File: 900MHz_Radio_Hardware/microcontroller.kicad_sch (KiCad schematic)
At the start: 7 parts, among them J1 RJ45_LED_Shielded, SW2 SW_SPDT, U2 Teensy4.1_DEV-16771, U7 MCP4725xxx-xCH

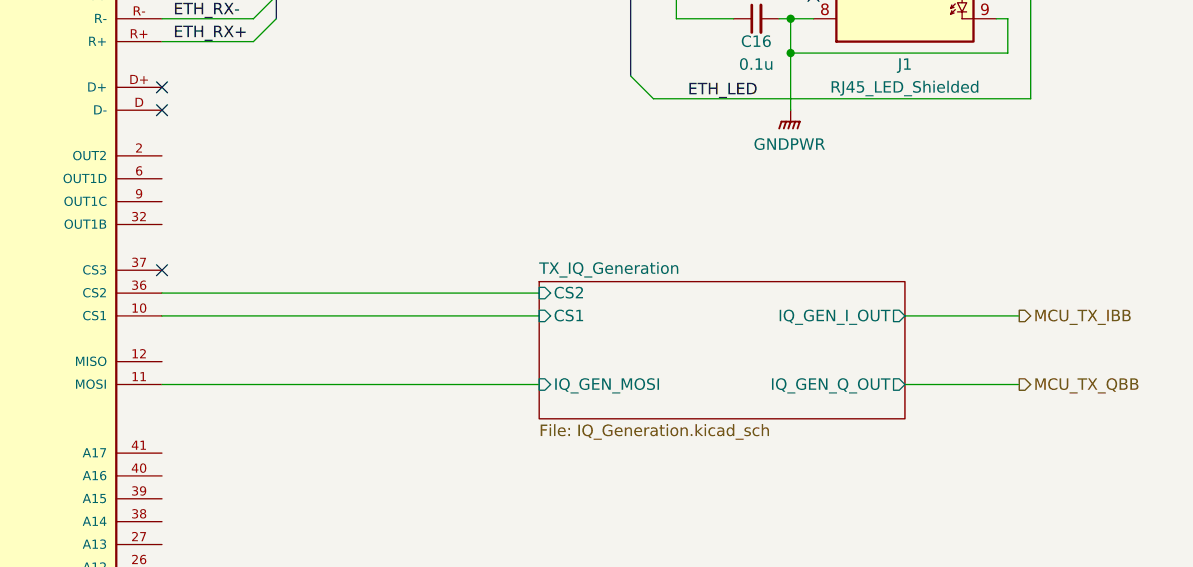
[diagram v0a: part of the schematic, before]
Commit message: Added modulator enable signal
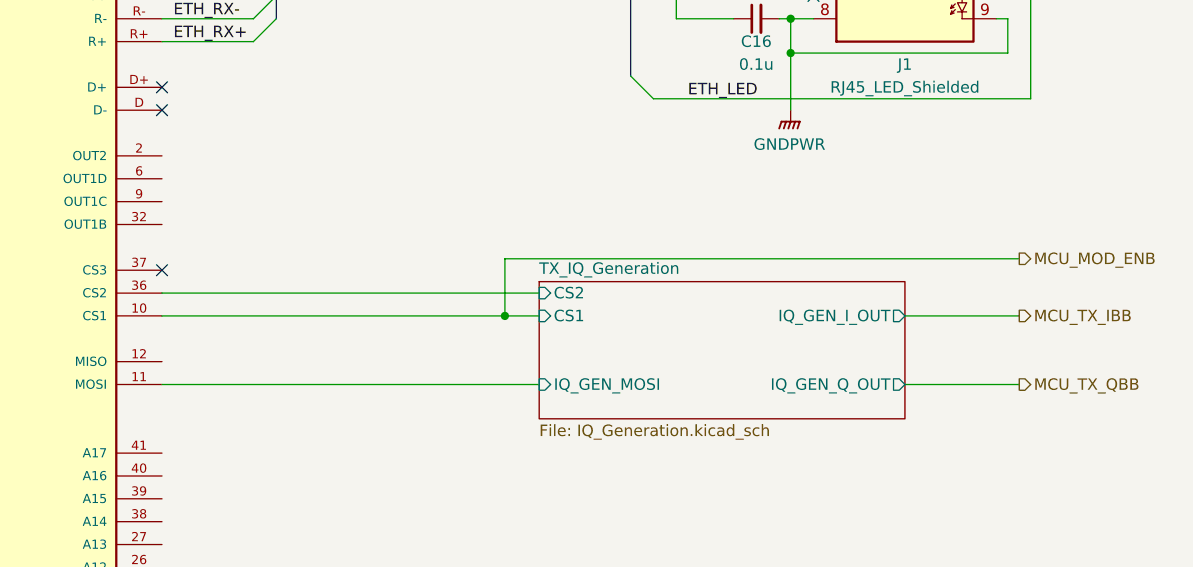
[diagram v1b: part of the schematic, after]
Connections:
- net TX_IQ_Generation/CS1 renamed MCU_MOD_ENB
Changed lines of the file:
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@@
   (junction (at 93.98 101.6) (diameter 0) (color 0 0 0 0)
+  )
+  (junction (at 205.74 76.2) (diameter 0) (color 0 0 0 0)
   )
   (junction (at 237.49 43.18) (diameter 0) (color 0 0 0 0)
@@
     (stroke (width 0) (type default))
   )
+  (wire (pts (xy 262.89 69.85) (xy 205.74 69.85))
+    (stroke (width 0) (type default))
+  )
   (wire (pts (xy 167.64 73.66) (xy 209.55 73.66))
     (stroke (width 0) (type default))
@@
     (stroke (width 0) (type default))
   )
+  (wire (pts (xy 205.74 76.2) (xy 209.55 76.2))
+    (stroke (width 0) (type default))
+  )
   (wire (pts (xy 236.22 43.18) (xy 237.49 43.18))
     (stroke (width 0) (type default))
@@
     (stroke (width 0) (type default))
   )
+  (wire (pts (xy 205.74 69.85) (xy 205.74 76.2))
+    (stroke (width 0) (type default))
+  )
   (wire (pts (xy 250.19 83.82) (xy 262.89 83.82))
     (stroke (width 0) (type default))
@@
     (stroke (width 0) (type default))
   )
-  (wire (pts (xy 167.64 76.2) (xy 209.55 76.2))
+  (wire (pts (xy 167.64 76.2) (xy 205.74 76.2))
     (stroke (width 0) (type default))
   )
@@
     (effects (font (size 1.27 1.27)) (justify right))
   )
+  (hierarchical_label "MCU_MOD_ENB" (shape output) (at 262.89 69.85 0) (fields_autoplaced)
+    (effects (font (size 1.27 1.27)) (justify left))
+  )
   (hierarchical_label "MCU_TX_QBB" (shape output) (at 262.89 83.82 0) (fields_autoplaced)

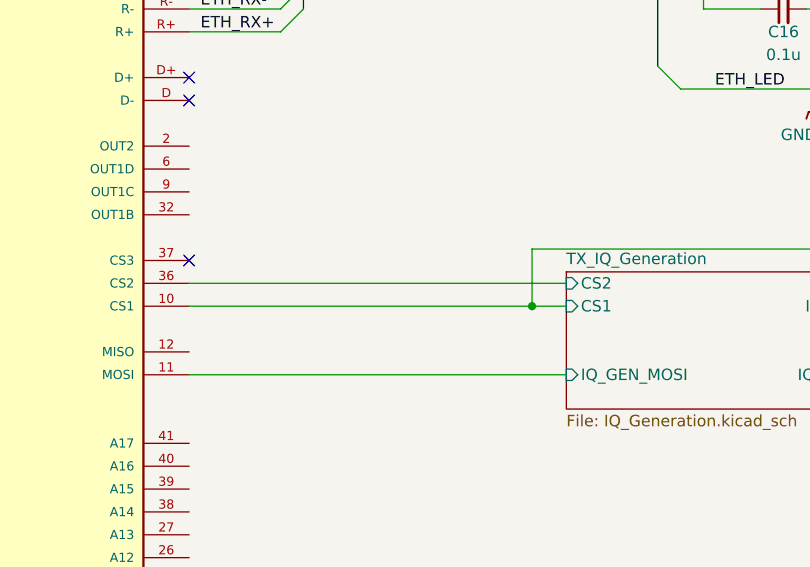
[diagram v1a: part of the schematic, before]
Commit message: Started fixing IQ gen circuit
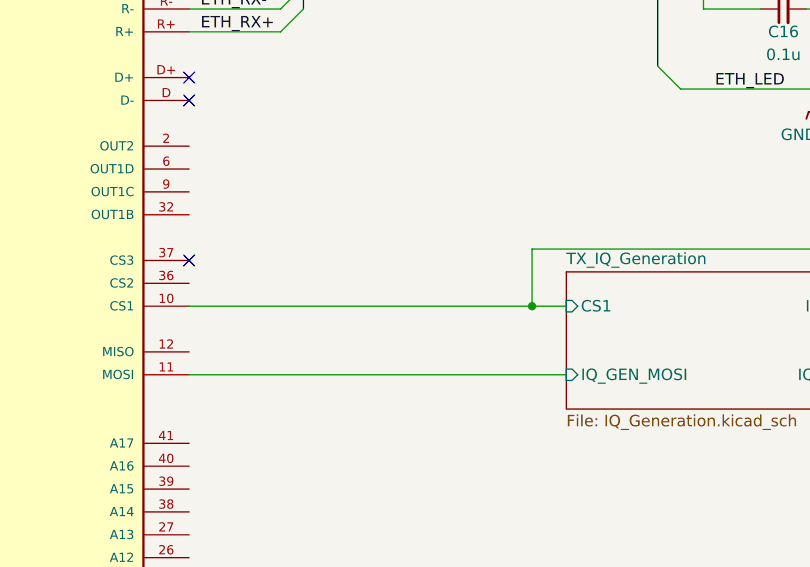
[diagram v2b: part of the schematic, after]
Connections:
- net TX_IQ_Generation/CS2: no longer names the net of U2.36 (CS2)
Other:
- sheet TX_IQ_Generation ports: added none; removed CS2
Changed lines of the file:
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@@
-    (stroke (width 0) (type default))
-  )
-  (wire (pts (xy 167.64 73.66) (xy 209.55 73.66))
     (stroke (width 0) (type default))
   )
@@
       (effects (font (size 1.27 1.27)) (justify left))
     )
-    (pin "CS2" input (at 209.55 73.66 180)
-      (effects (font (size 1.27 1.27)) (justify left))
-    )

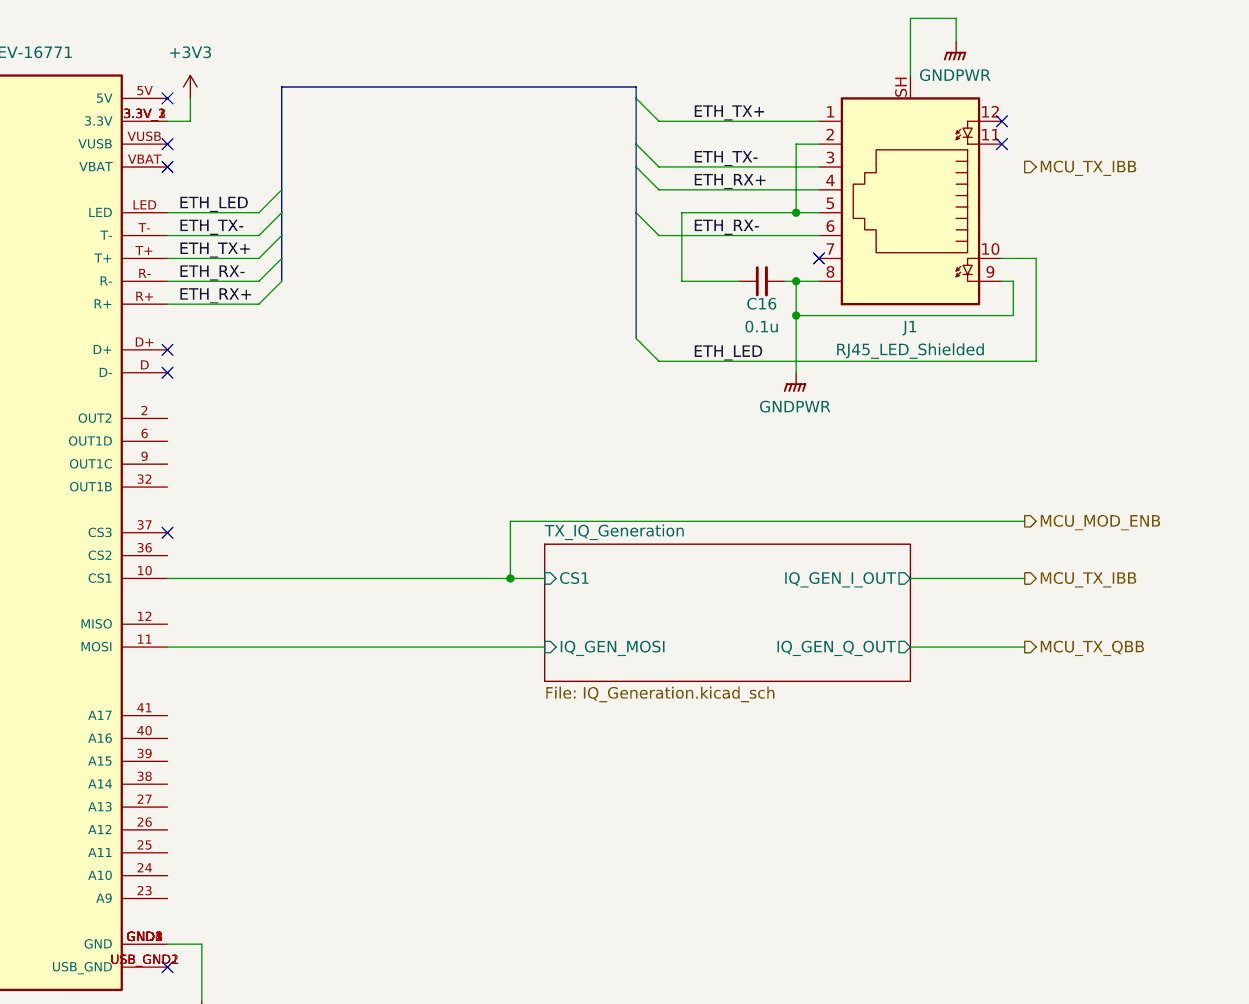
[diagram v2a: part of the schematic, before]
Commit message: Replaced DAC
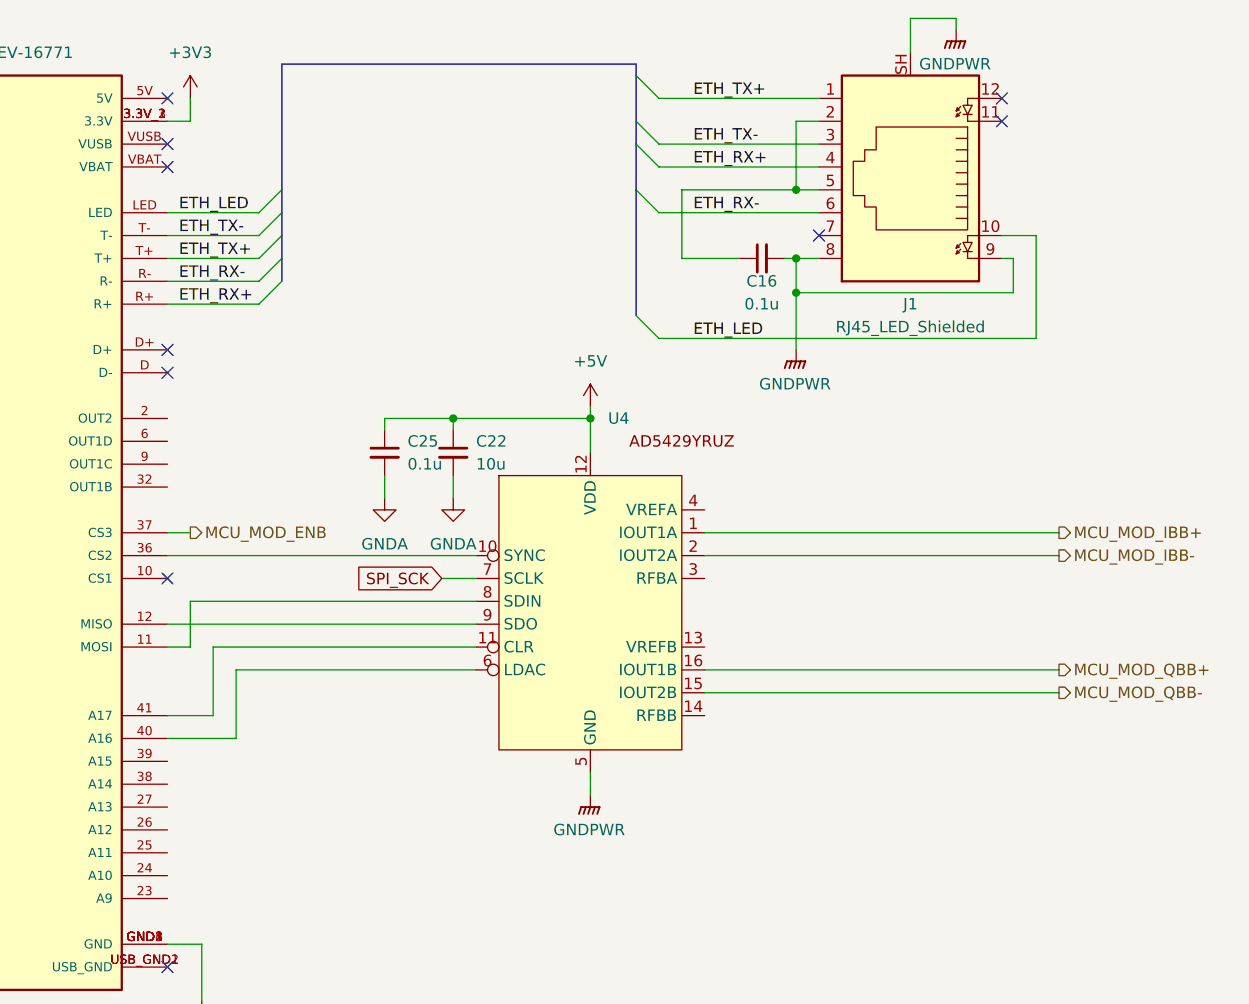
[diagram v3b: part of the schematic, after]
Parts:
- added C22: 10u, symbol Device:C_Small
- added C25: 0.1u, symbol Device:C_Small
- added U4: ~, Package_SO:TSSOP-16_4.4x5mm_P0.65mm, symbol MRDT_ICs:AD5429YRUZ
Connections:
- net +5V: now also C22.1, C25.1, U4.12 (VDD)
- net GNDPWR: now also U4.5 (GND)
- net MCU_MOD_ENB: now also U2.37 (CS3); no longer U2.10 (CS1)
- net SPI_SCK: now also U4.7 (SCLK)
- net at U2.12 (MISO): now also U4.9 (SDO)
- net at U2.36 (CS2): now also U4.10 (SYNC)
- net at U2.40 (A16): now also U4.6 (LDAC)
- net at U2.41 (A17): now also U4.11 (CLR)
- net TX_IQ_Generation/IQ_GEN_MOSI: no longer names the net of U2.11 (MOSI)
- net TX_IQ_Generation/IQ_GEN_MOSI: now also U4.8 (SDIN)
- new net GNDA: C22.2, C25.2
- new net MCU_MOD_IBB+: U4.1 (IOUT1A)
- new net MCU_MOD_IBB-: U4.2 (IOUT2A)
- new net MCU_MOD_QBB+: U4.16 (IOUT1B)
- new net MCU_MOD_QBB-: U4.15 (IOUT2B)
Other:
- removed sheet TX_IQ_Generation
- moved on the sheet: C16, J1

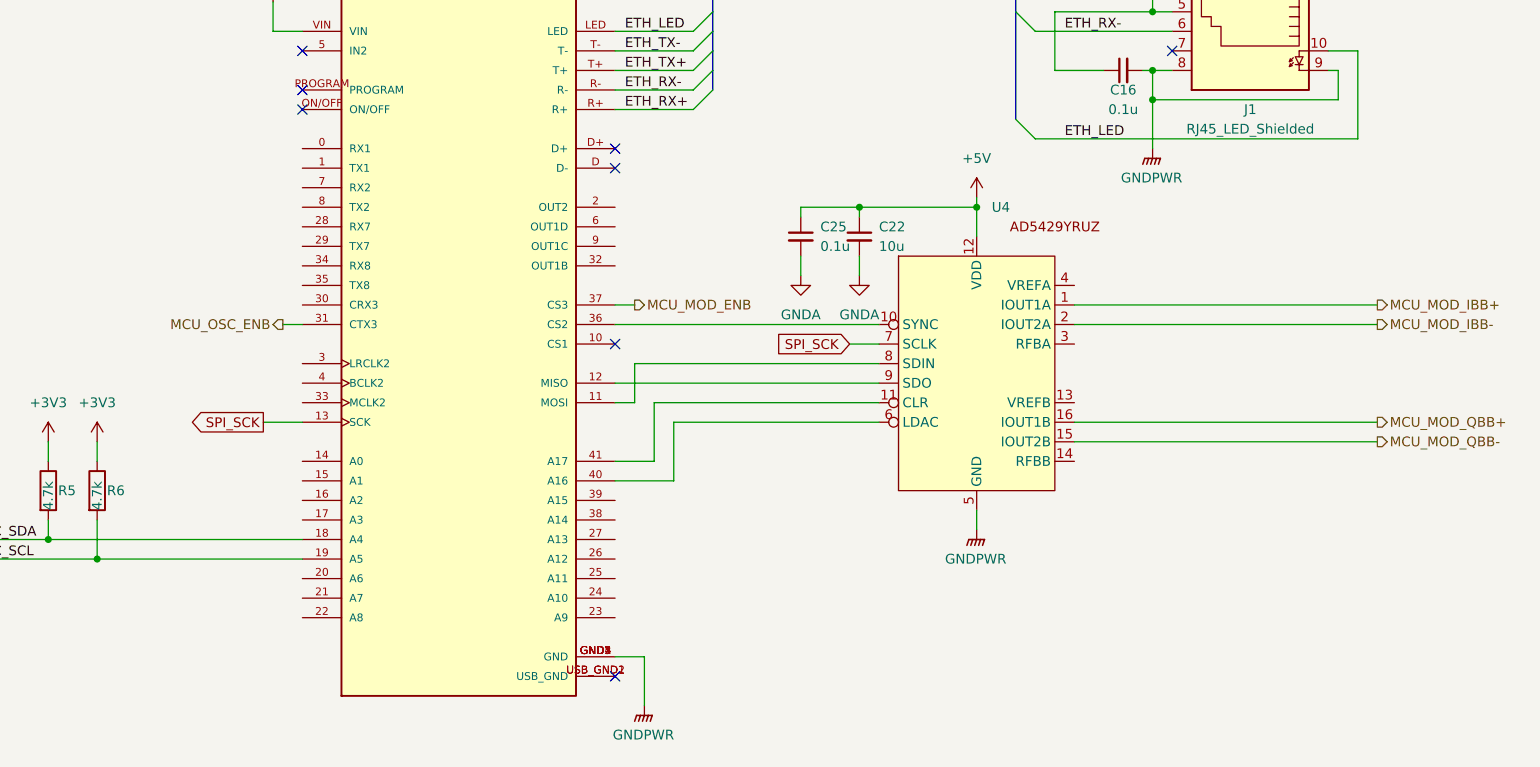
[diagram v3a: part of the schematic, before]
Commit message: Started demodulator
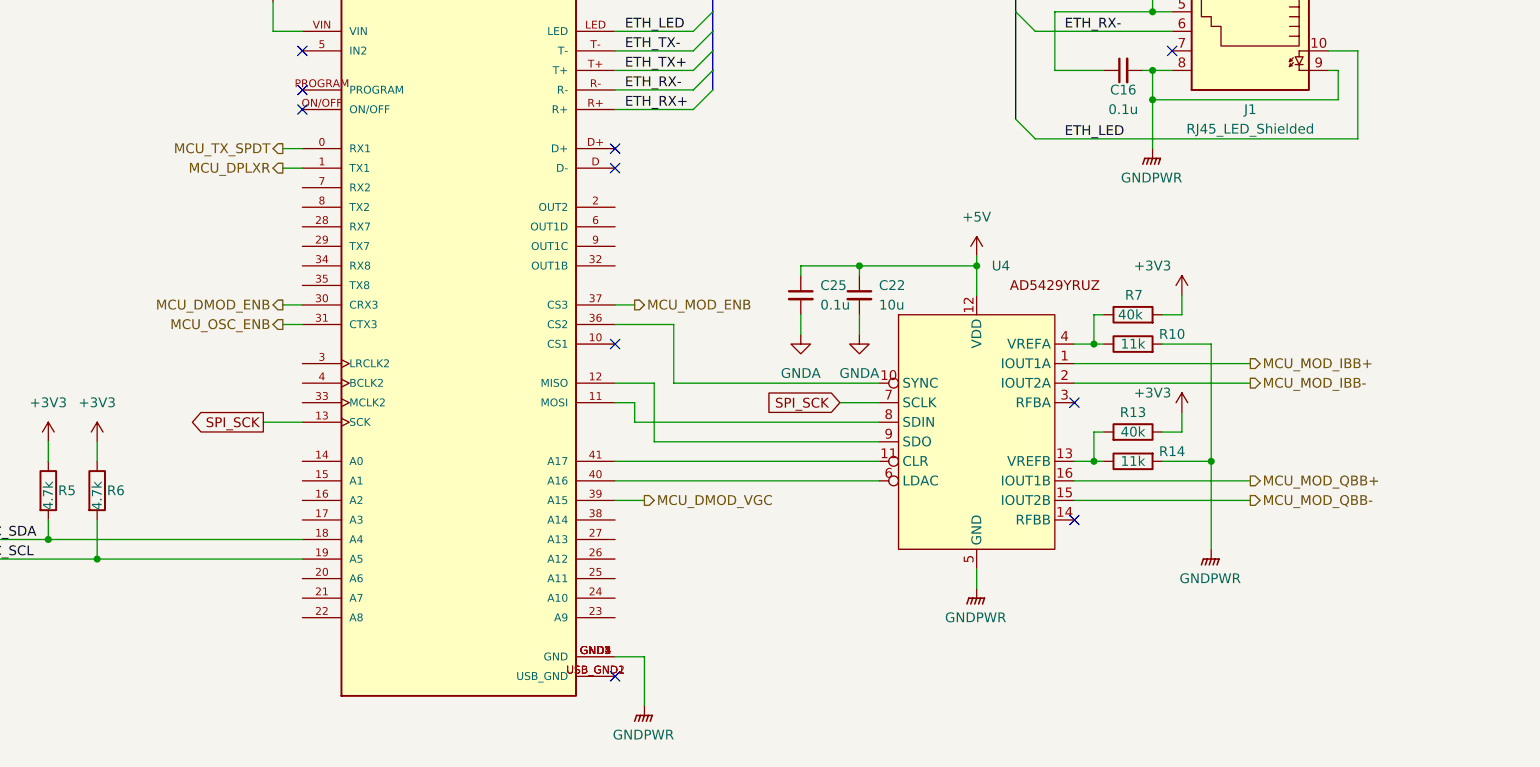
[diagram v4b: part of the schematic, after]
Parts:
- added R10, R14: 11k, symbol Device:R
- added R13, R7: 40k, symbol Device:R
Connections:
- net +3V3: now also R13.1, R7.2
- net GNDPWR: now also R10.2, R14.2
- net at U4.13 (VREFB): now also R13.2, R14.1
- net at U4.4 (VREFA): now also R10.1, R7.1
- net MCU_TX_SPDT: now reaches U2.0 (RX1)
- net MCU_DPLXR: now reaches U2.1 (TX1)
- net MCU_DMOD_ENB: now reaches U2.30 (CRX3)
- net MCU_DMOD_VGC: now reaches U2.39 (A15)
- no-connect marks 13 -> 15
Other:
- moved on the sheet: C22, C25, U4
